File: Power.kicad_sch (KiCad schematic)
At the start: 18 parts, among them U1 AMS1117-5.0, U2 AMS1117-3.3, X1 PEDAL_COMBO_TOP

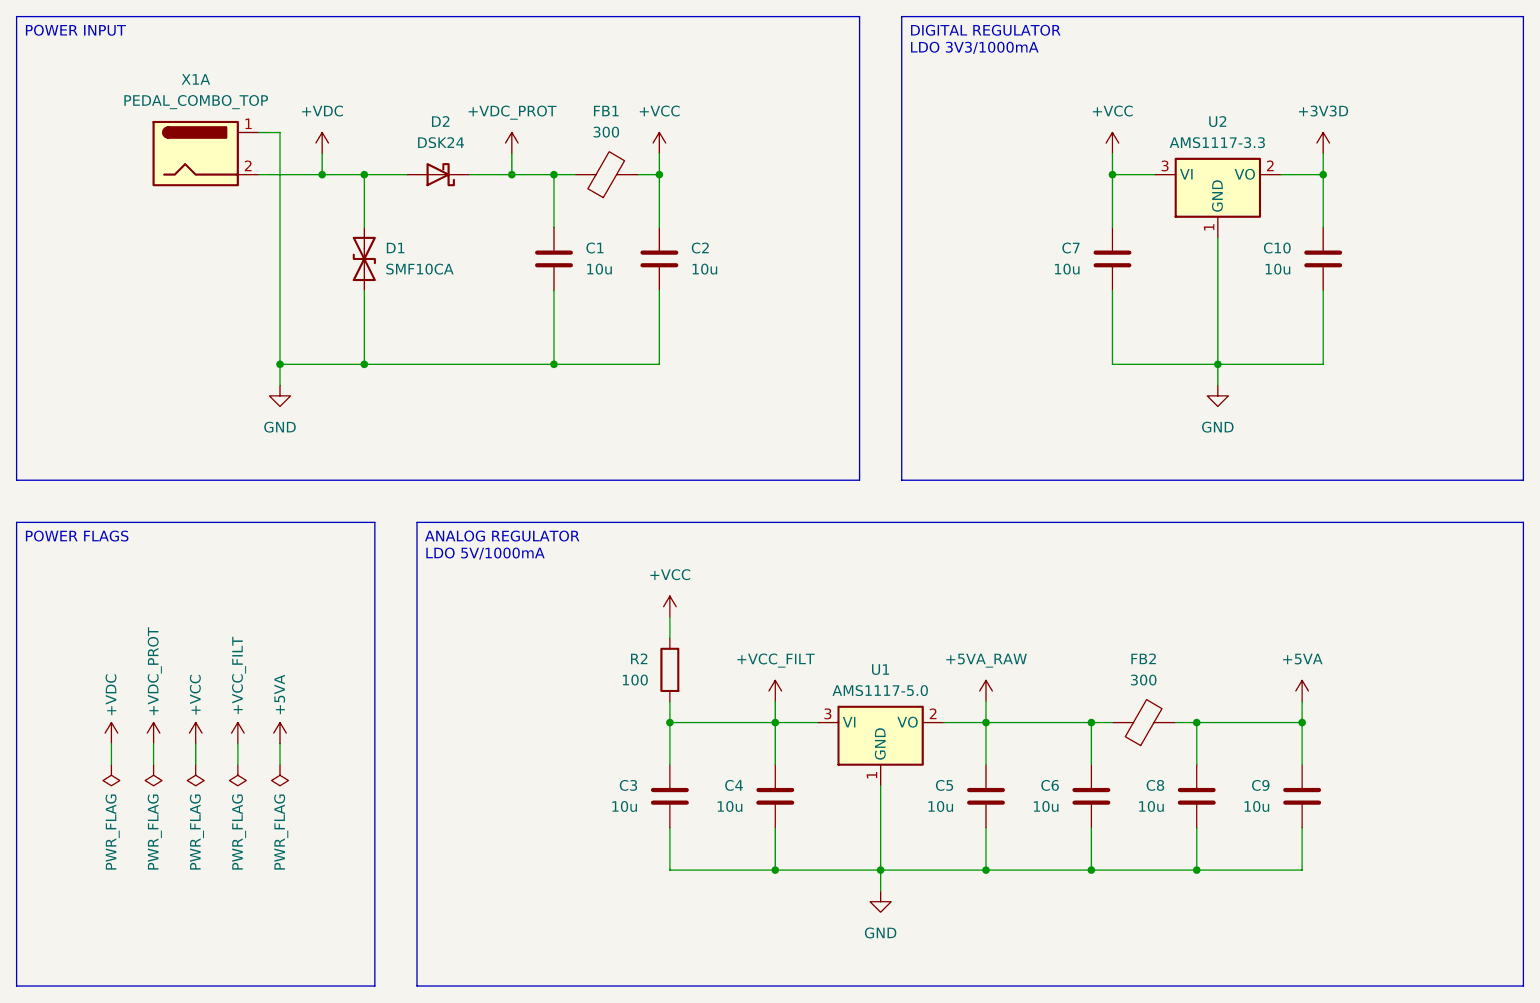
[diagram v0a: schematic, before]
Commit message: Layout and power supply filtering
Updated the board layout.
Updated the project to KiCad 10.0.
Added additional power supply filtering.
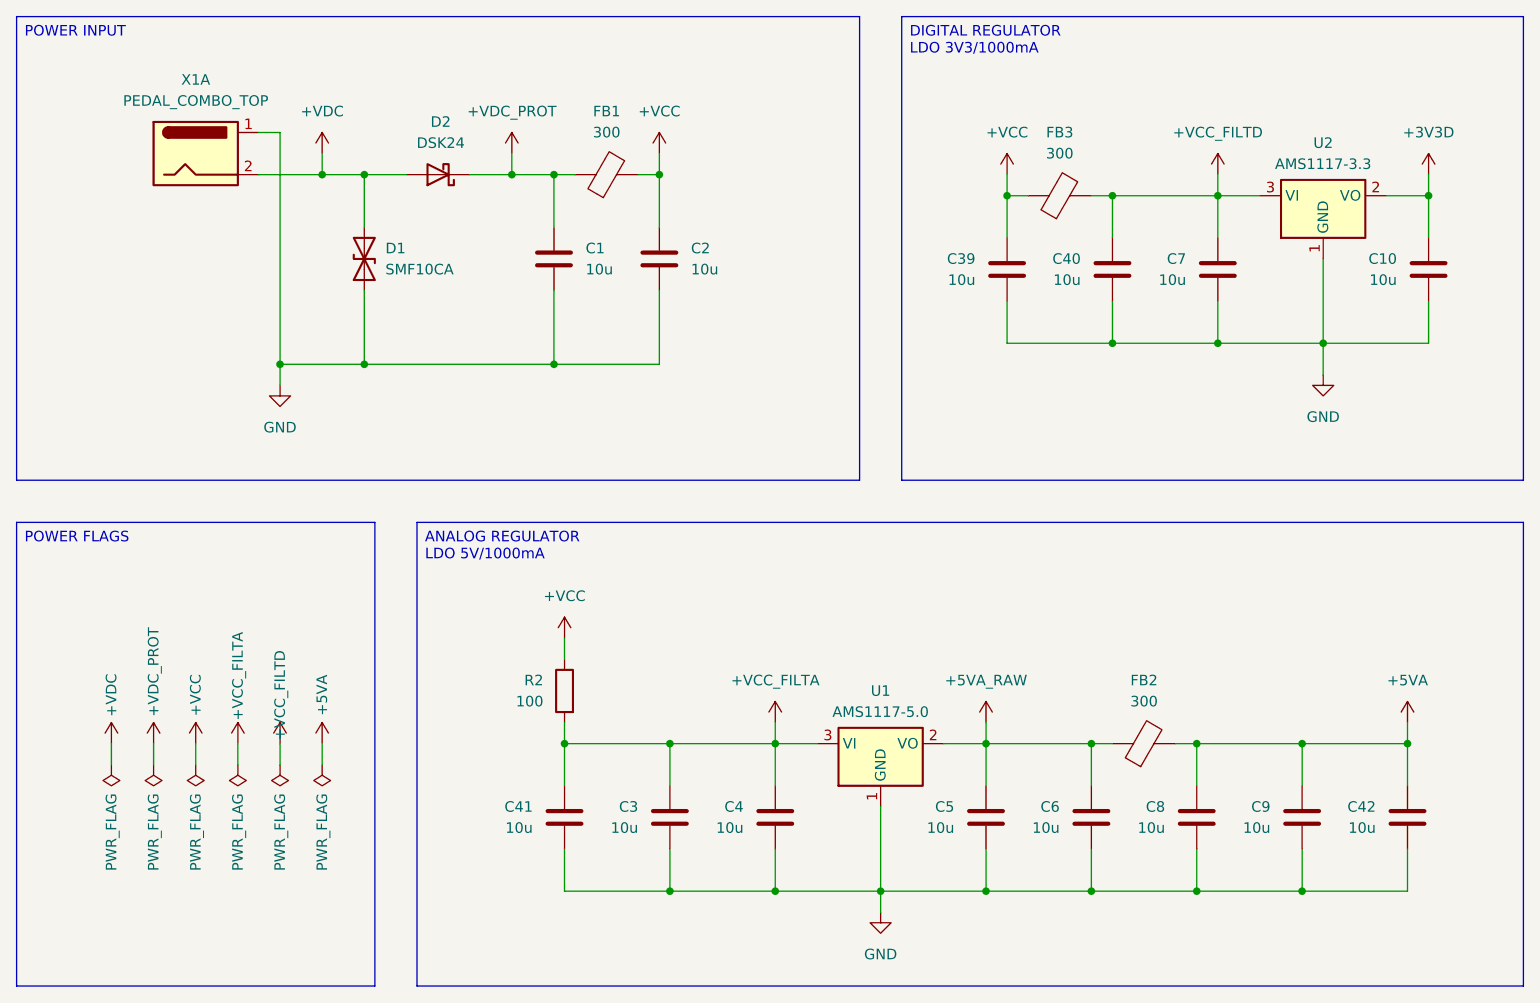
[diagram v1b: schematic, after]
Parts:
- added C39, C40, C41, C42: 10u, Capacitor_SMD:C_0805_2012Metric, symbol Device:C
- added FB3: 300, Inductor_SMD:L_0603_1608Metric, symbol Device:FerriteBead
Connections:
- net +5VA: now also C42.1
- net +VCC: now also C39.1, FB3.1; no longer C7.1, U2.3 (VI)
- net GND: now also C39.2, C40.2, C41.2, C42.2
- net +VCC_FILT renamed +VCC_FILTA
- net +VCC_FILTA: now also C41.1
- new net +VCC_FILTD: C40.1, C7.1, FB3.2, U2.3 (VI)
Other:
- moved on the sheet: C10, C3, C4, C5, C6, C7, C8, C9, FB2, R2, U1, U2
